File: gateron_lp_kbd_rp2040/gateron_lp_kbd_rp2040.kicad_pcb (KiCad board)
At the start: 2 copper layers, 234.5 x 116.5 mm, 244 parts, among them J1 TYPE-C-31-M-12, J2 Battery JST-SH, Q1 DMG3415U, SW1 KS-33, SW10 KS-33, SW11 KS-33, SW12 KS-33, SW13 KS-33, SW14 KS-33, SW15 KS-33, SW16 KS-33, SW17 KS-33, SW18 KS-33, SW19 KS-33, SW2 KS-33, SW20 KS-33, SW21 KS-33, SW22 KS-33, SW23 KS-33, SW24 KS-33, SW25 KS-33, SW26 KS-33, SW27 KS-33, SW28 KS-33, SW29 KS-33, SW3 KS-33, SW30 KS-33, SW31 KS-33, SW32 KS-33, SW33 KS-33, SW34 KS-33, SW35 KS-33, SW36 KS-33, SW37 KS-33, SW38 KS-33, SW39 KS-33, SW4 KS-33, SW40 KS-33, SW41 KS-33, SW42 KS-33, SW43 KS-33, SW44 KS-33, SW45 KS-33, SW46 KS-33, SW47 KS-33, SW48 KS-33, SW49 KS-33, SW5 KS-33, SW50 KS-33, SW51 KS-33, SW52 KS-33, SW53 KS-33, SW54 KS-33, SW55 KS-33, SW56 KS-33, SW57 KS-33, SW58 KS-33, SW59 KS-33, SW6 KS-33, SW60 RESET, SW61 BOOTSEL, SW62 PWR MSK-12C02, SW7 KS-33, SW8 KS-33, SW9 KS-33, U1 RP2040, U2 MCP73831, U3 AP2112K-3.3, U4 USBLC6-2SC6, U5 W25Q16JVUXIQ, U6 CYW43439, U7 74AHCT1G125, Y1 12MHz, Y2 37.4MHz

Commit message: Ground CYW43439 antenna matching in Raspberry Pi's real Pico W design
Cross-checked L2/C17/C18 and the crystal load caps against Raspberry Pi's
public Pico W hardware design files (same CYW43439 die, confirms 37.4MHz).
Real component families found there: 4.7nH match inductor, 27pF crystal
load caps, and a documented 0.2-2pF antenna tuning-cap family -- Pico W's
own BOM shows even Raspberry Pi tunes this network per-board rather than
using one fixed value, so C18 is left DNP pending real tuning here too.

Co-Authored-By: Claude Sonnet 5 <noreply@anthropic.com>
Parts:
- C17: value DNP (VERIFY) -> 1p (VERIFY, tune 0.2-2p)
- C18: value DNP (VERIFY) -> DNP (VERIFY, tune)
- C30, C31: value 18p -> 27p
- L2: value DNP (VERIFY) -> 4.7nH (ref: Pico W)
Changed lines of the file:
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@@
     (effects (font (size 1 1) (thickness 0.15)))
   )
-  (property "Value" "18p" (at 0 1.5 0) (layer "F.Fab")
+  (property "Value" "27p" (at 0 1.5 0) (layer "F.Fab")
     (effects (font (size 1 1) (thickness 0.15)))
   )
@@
     (effects (font (size 1 1) (thickness 0.15)))
   )
-  (property "Value" "18p" (at 0 1.5 0) (layer "F.Fab")
+  (property "Value" "27p" (at 0 1.5 0) (layer "F.Fab")
     (effects (font (size 1 1) (thickness 0.15)))
   )
@@
     (effects (font (size 1 1) (thickness 0.15)))
   )
-  (property "Value" "DNP (VERIFY)" (at 0 1.5 270) (layer "F.Fab")
+  (property "Value" "4.7nH (ref: Pico W)" (at 0 1.5 270) (layer "F.Fab")
     (effects (font (size 1 1) (thickness 0.15)))
   )
@@
     (effects (font (size 1 1) (thickness 0.15)))
   )
-  (property "Value" "DNP (VERIFY)" (at 0 1.5 0) (layer "F.Fab")
+  (property "Value" "1p (VERIFY, tune 0.2-2p)" (at 0 1.5 0) (layer "F.Fab")
     (effects (font (size 1 1) (thickness 0.15)))
   )
@@
     (effects (font (size 1 1) (thickness 0.15)))
   )
-  (property "Value" "DNP (VERIFY)" (at 0 1.5 0) (layer "F.Fab")
+  (property "Value" "DNP (VERIFY, tune)" (at 0 1.5 0) (layer "F.Fab")
     (effects (font (size 1 1) (thickness 0.15)))
   )

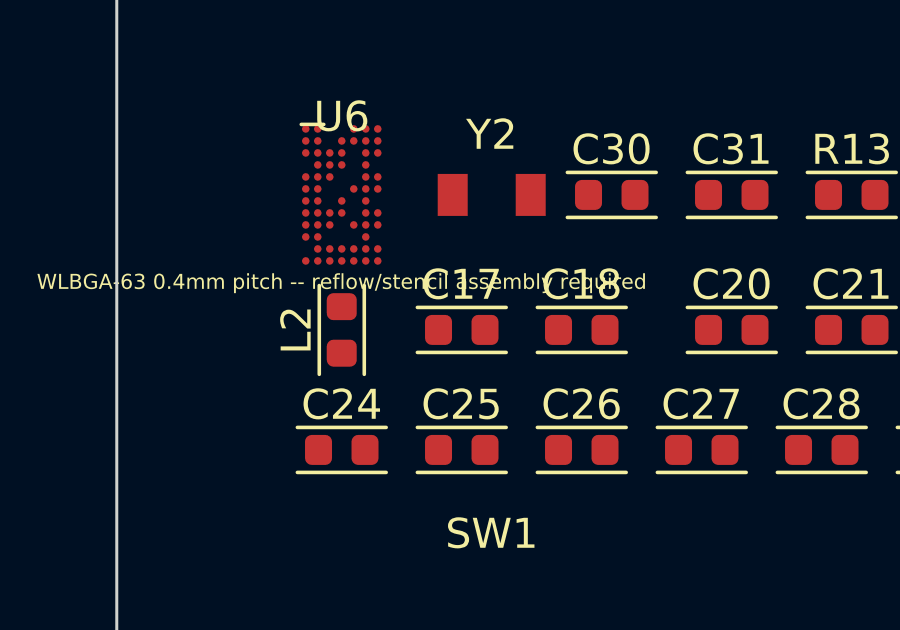
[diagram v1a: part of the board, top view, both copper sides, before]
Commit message: Match antenna-network footprints to real component package sizes
L2/C17/C18 were using the generic 0603-imperial footprint shared by this
file's other passives, but the real Pico W reference parts are smaller:
the antenna-match inductor is 0201 imperial (Murata LQP03TN4N7H02D, the
DigiKey-listed substitute for the now-obsolete Cyntec original) and the
Murata GJM1555C1H tuning-cap family is 0402 imperial. Added fp_0201/
fp_0402 land patterns and switched L2 to 0201, C17/C18 to 0402.

Co-Authored-By: Claude Sonnet 5 <noreply@anthropic.com>
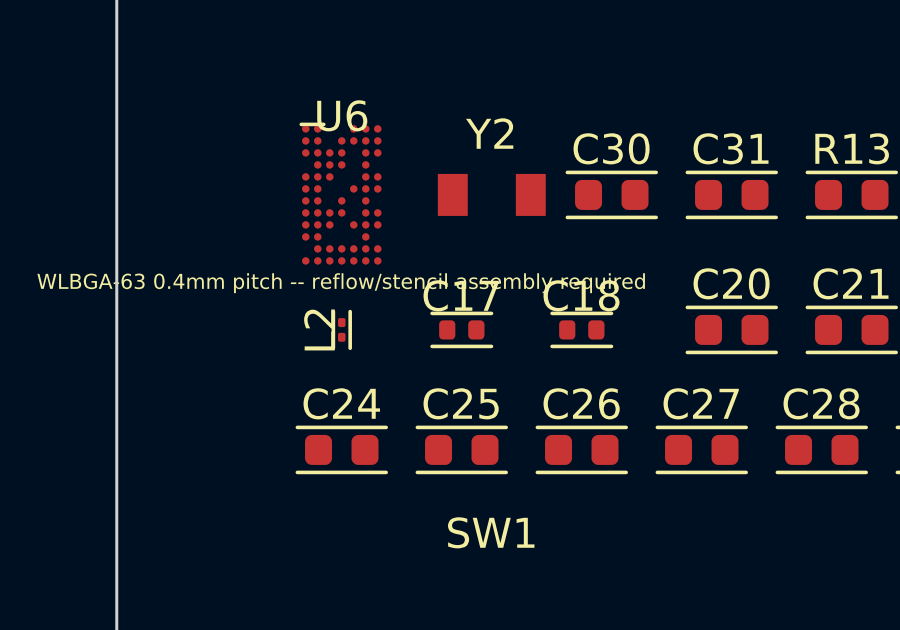
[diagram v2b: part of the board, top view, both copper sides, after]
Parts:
- C17, C18: footprint kbd:RC_0603 -> kbd:RC_0402
- L2: footprint kbd:RC_0603 -> kbd:RC_0201
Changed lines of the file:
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@@
     (fp_rect (start -1.5 -0.9) (end 1.5 0.9) (stroke (width 0.05) (type solid)) (fill none) (layer "F.CrtYd"))
   )
-  (footprint "kbd:RC_0603" (layer "F.Cu")
+  (footprint "kbd:RC_0201" (layer "F.Cu")
   (at 45 34.5 90)
-  (property "Reference" "L2" (at 0 -1.5 270) (layer "F.SilkS")
+  (property "Reference" "L2" (at 0 -0.7 270) (layer "F.SilkS")
     (effects (font (size 1 1) (thickness 0.15)))
   )
-  (property "Value" "4.7nH (ref: Pico W)" (at 0 1.5 270) (layer "F.Fab")
+  (property "Value" "4.7nH (ref: Pico W)" (at 0 0.7 270) (layer "F.Fab")
     (effects (font (size 1 1) (thickness 0.15)))
   )
-  (property "Footprint" "kbd:RC_0603" (at 0 0 0) (layer "F.Fab") (hide yes)
+  (property "Footprint" "kbd:RC_0201" (at 0 0 0) (layer "F.Fab") (hide yes)
     (effects (font (size 1.27 1.27))))
   (property "Datasheet" "" (at 0 0 0) (layer "F.Fab") (hide yes)
@@
     (effects (font (size 1.27 1.27))))
   (attr smd)
-    (pad "1" smd roundrect (at -0.775 0 90) (size 0.9 1) (layers "F.Cu" "F.Paste" "F.Mask") (net 46 "WLRF_ANT") (roundrect_rratio 0.25))
-    (pad "2" smd roundrect (at 0.775 0 90) (size 0.9 1) (layers "F.Cu" "F.Paste" "F.Mask") (net 47 "WLRF_ANT_MID") (roundrect_rratio 0.25))
-    (fp_rect (start -0.8 -0.4) (end 0.8 0.4) (stroke (width 0.1) (type solid)) (fill none) (layer "F.Fab"))
-    (fp_line (start -1.48 -0.75) (end 1.48 -0.75) (stroke (width 0.12) (type solid)) (layer "F.SilkS"))
-    (fp_line (start -1.48 0.75) (end 1.48 0.75) (stroke (width 0.12) (type solid)) (layer "F.SilkS"))
-    (fp_rect (start -1.5 -0.9) (end 1.5 0.9) (stroke (width 0.05) (type solid)) (fill none) (layer "F.CrtYd"))
+    (pad "1" smd roundrect (at -0.245 0 90) (size 0.3 0.25) (layers "F.Cu" "F.Paste" "F.Mask") (net 46 "WLRF_ANT") (roundrect_rratio 0.25))
+    (pad "2" smd roundrect (at 0.245 0 90) (size 0.3 0.25) (layers "F.Cu" "F.Paste" "F.Mask") (net 47 "WLRF_ANT_MID") (roundrect_rratio 0.25))
+    (fp_rect (start -0.3 -0.15) (end 0.3 0.15) (stroke (width 0.1) (type solid)) (fill none) (layer "F.Fab"))
+    (fp_line (start -0.61 -0.28) (end 0.61 -0.28) (stroke (width 0.12) (type solid)) (layer "F.SilkS"))
+    (fp_line (start -0.61 0.28) (end 0.61 0.28) (stroke (width 0.12) (type solid)) (layer "F.SilkS"))
+    (fp_rect (start -0.61 -0.33) (end 0.61 0.33) (stroke (width 0.05) (type solid)) (fill none) (layer "F.CrtYd"))
   )
-  (footprint "kbd:RC_0603" (layer "F.Cu")
+  (footprint "kbd:RC_0402" (layer "F.Cu")
   (at 49 34.5)
-  (property "Reference" "C17" (at 0 -1.5 0) (layer "F.SilkS")
+  (property "Reference" "C17" (at 0 -1.1 0) (layer "F.SilkS")
     (effects (font (size 1 1) (thickness 0.15)))
   )
-  (property "Value" "1p (VERIFY, tune 0.2-2p)" (at 0 1.5 0) (layer "F.Fab")
+  (property "Value" "1p (VERIFY, tune 0.2-2p)" (at 0 1.1 0) (layer "F.Fab")
     (effects (font (size 1 1) (thickness 0.15)))
   )
-  (property "Footprint" "kbd:RC_0603" (at 0 0 0) (layer "F.Fab") (hide yes)
+  (property "Footprint" "kbd:RC_0402" (at 0 0 0) (layer "F.Fab") (hide yes)
     (effects (font (size 1.27 1.27))))
   (property "Datasheet" "" (at 0 0 0) (layer "F.Fab") (hide yes)
@@
     (effects (font (size 1.27 1.27))))
   (attr smd)
-    (pad "1" smd roundrect (at -0.775 0) (size 0.9 1) (layers "F.Cu" "F.Paste" "F.Mask") (net 46 "WLRF_ANT") (roundrect_rratio 0.25))
-    (pad "2" smd roundrect (at 0.775 0) (size 0.9 1) (layers "F.Cu" "F.Paste" "F.Mask") (net 1 "GND") (roundrect_rratio 0.25))
-    (fp_rect (start -0.8 -0.4) (end 0.8 0.4) (stroke (width 0.1) (type solid)) (fill none) (layer "F.Fab"))
-    (fp_line (start -1.48 -0.75) (end 1.48 -0.75) (stroke (width 0.12) (type solid)) (layer "F.SilkS"))
-    (fp_line (start -1.48 0.75) (end 1.48 0.75) (stroke (width 0.12) (type solid)) (layer "F.SilkS"))
-    (fp_rect (start -1.5 -0.9) (end 1.5 0.9) (stroke (width 0.05) (type solid)) (fill none) (layer "F.CrtYd"))
+    (pad "1" smd roundrect (at -0.485 0) (size 0.54 0.64) (layers "F.Cu" "F.Paste" "F.Mask") (net 46 "WLRF_ANT") (roundrect_rratio 0.25))
+    (pad "2" smd roundrect (at 0.485 0) (size 0.54 0.64) (layers "F.Cu" "F.Paste" "F.Mask") (net 1 "GND") (roundrect_rratio 0.25))
+    (fp_rect (start -0.5 -0.25) (end 0.5 0.25) (stroke (width 0.1) (type solid)) (fill none) (layer "F.Fab"))
+    (fp_line (start -0.99 -0.55) (end 0.99 -0.55) (stroke (width 0.12) (type solid)) (layer "F.SilkS"))
+    (fp_line (start -0.99 0.55) (end 0.99 0.55) (stroke (width 0.12) (type solid)) (layer "F.SilkS"))
+    (fp_rect (start -1 -0.6) (end 1 0.6) (stroke (width 0.05) (type solid)) (fill none) (layer "F.CrtYd"))
   )
-  (footprint "kbd:RC_0603" (layer "F.Cu")
+  (footprint "kbd:RC_0402" (layer "F.Cu")
   (at 53 34.5)
-  (property "Reference" "C18" (at 0 -1.5 0) (layer "F.SilkS")
+  (property "Reference" "C18" (at 0 -1.1 0) (layer "F.SilkS")
     (effects (font (size 1 1) (thickness 0.15)))
   )
-  (property "Value" "DNP (VERIFY, tune)" (at 0 1.5 0) (layer "F.Fab")
+  (property "Value" "DNP (VERIFY, tune)" (at 0 1.1 0) (layer "F.Fab")
     (effects (font (size 1 1) (thickness 0.15)))
   )
-  (property "Footprint" "kbd:RC_0603" (at 0 0 0) (layer "F.Fab") (hide yes)
+  (property "Footprint" "kbd:RC_0402" (at 0 0 0) (layer "F.Fab") (hide yes)
     (effects (font (size 1.27 1.27))))
   (property "Datasheet" "" (at 0 0 0) (layer "F.Fab") (hide yes)
@@
     (effects (font (size 1.27 1.27))))
   (attr smd)
-    (pad "1" smd roundrect (at -0.775 0) (size 0.9 1) (layers "F.Cu" "F.Paste" "F.Mask") (net 47 "WLRF_ANT_MID") (roundrect_rratio 0.25))
-    (pad "2" smd roundrect (at 0.775 0) (size 0.9 1) (layers "F.Cu" "F.Paste" "F.Mask") (net 1 "GND") (roundrect_rratio 0.25))
-    (fp_rect (start -0.8 -0.4) (end 0.8 0.4) (stroke (width 0.1) (type solid)) (fill none) (layer "F.Fab"))
-    (fp_line (start -1.48 -0.75) (end 1.48 -0.75) (stroke (width 0.12) (type solid)) (layer "F.SilkS"))
-    (fp_line (start -1.48 0.75) (end 1.48 0.75) (stroke (width 0.12) (type solid)) (layer "F.SilkS"))
-    (fp_rect (start -1.5 -0.9) (end 1.5 0.9) (stroke (width 0.05) (type solid)) (fill none) (layer "F.CrtYd"))
+    (pad "1" smd roundrect (at -0.485 0) (size 0.54 0.64) (layers "F.Cu" "F.Paste" "F.Mask") (net 47 "WLRF_ANT_MID") (roundrect_rratio 0.25))
+    (pad "2" smd roundrect (at 0.485 0) (size 0.54 0.64) (layers "F.Cu" "F.Paste" "F.Mask") (net 1 "GND") (roundrect_rratio 0.25))
+    (fp_rect (start -0.5 -0.25) (end 0.5 0.25) (stroke (width 0.1) (type solid)) (fill none) (layer "F.Fab"))
+    (fp_line (start -0.99 -0.55) (end 0.99 -0.55) (stroke (width 0.12) (type solid)) (layer "F.SilkS"))
+    (fp_line (start -0.99 0.55) (end 0.99 0.55) (stroke (width 0.12) (type solid)) (layer "F.SilkS"))
+    (fp_rect (start -1 -0.6) (end 1 0.6) (stroke (width 0.05) (type solid)) (fill none) (layer "F.CrtYd"))
   )
   (footprint "kbd:RC_0603" (layer "F.Cu")

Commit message: Confirm crystal load caps and series resistor against Pico W reference
C30/C31 (27pF) and R13 (0R) were already set to these values but flagged
VERIFY -- re-checked against Raspberry Pi's public Pico W design files
with reference-designator-level evidence this time (not just proximity in
the raw dump): C257/C258 map 1:1 to the 27pF footprint, exactly the pair
a crystal load network needs, and a 0R chip resistor sits on the wireless
chip's crystal clock net. 27pF externals also check out physically
(~15.5-18.5pF effective load cap with typical stray, a standard CL rating).
No value changes, just upgraded confidence and updated comments.

Co-Authored-By: Claude Sonnet 5 <noreply@anthropic.com>
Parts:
- R13: value 0 (VERIFY) -> 0 (ref: Pico W)
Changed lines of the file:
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@@
     (effects (font (size 1 1) (thickness 0.15)))
   )
-  (property "Value" "0 (VERIFY)" (at 0 1.5 0) (layer "F.Fab")
+  (property "Value" "0 (ref: Pico W)" (at 0 1.5 0) (layer "F.Fab")
     (effects (font (size 1 1) (thickness 0.15)))
   )

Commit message: Verify RP2040 pin numbers against the real datasheet, fix two real bugs
Pin numbers, dedicated-pin names, and QFN-56 side rotation now come from
Raspberry Pi's own RP2040 datasheet (Fig. 3, Table 1, Table 2) instead of
an invented sequential scheme. This caught two real design bugs:

- The core supply was modeled as a buck regulator needing an external
  inductor (L1, 2.2uH). The real on-chip regulator (Section 2.10, "Core
  Supply Regulator") is a linear/LDO type -- VREG_VIN -> VREG_VOUT -> DVDD
  -- needing only decoupling capacitors. L1 is removed; C9/C32/C33/C34 now
  match the datasheet's own application circuit (Figure 20).
- The BT UART was wired to GPIO18-21, but UART1's real alternate-function
  pins are GPIO20-23 (Table 2) -- GPIO18/19 (no alt-function needed) now
  carry BT_REG_ON/BT_DEV_WAKE instead, freeing GPIO20-23 for the actual
  UART1 TX/RX/CTS/RTS.

Also fixed: the real chip has no perimeter GND pins (GND is only the
single exposed thermal pad) -- removed several invented ones. And caught,
independently of the pinout work, two schematic label collisions (C13/C14
and C30/C31 crystal load caps landing global labels of different nets on
the identical coordinate, which can short a net to GND in the extracted
netlist) -- widened spacing to fix both.

Verified via kicad-happy analyzers: zero new errors/warnings, zero
courtyard or keepout collisions, zero schematic label collisions anywhere
in the file (full-file scan, not just the touched areas).

Co-Authored-By: Claude Sonnet 5 <noreply@anthropic.com>
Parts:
- removed L1: 2.2uH, kbd:RC_0603
- added C32: 100n, kbd:RC_0603, F.Cu at (164.0, 24.5)
- added C33: 100n, kbd:RC_0603, F.Cu at (168.0, 24.5)
- added C34: 1u, kbd:RC_0603, F.Cu at (172.0, 24.5)
- C9: value 10u -> 1u
- moved C10 8.00 mm to (176.0, 24.5)
- moved C11 8.00 mm to (180.0, 24.5)
- moved C12 8.00 mm to (188.0, 24.5)
- moved R9 8.00 mm to (184.0, 24.5)
- moved C9 4.00 mm to (160.0, 24.5)
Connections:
- C9 pad 1: VDD_CORE -> DVDD
- U1 pad 1: ROW0 -> +3V3
- U1 pad 10: COL4 -> +3V3
- U1 pad 11: COL5 -> COL3
- U1 pad 12: COL6 -> COL4
- U1 pad 13: COL7 -> COL5
- U1 pad 14: COL8 -> COL6
- U1 pad 15: COL9 -> COL7
- U1 pad 16: COL10 -> COL8
- U1 pad 17: COL11 -> COL9
- U1 pad 18: RGB_GPIO -> COL10
- U1 pad 2: ROW1 -> ROW0
- U1 pad 20: GND -> XIN
- U1 pad 21: USB_DM -> XOUT
- U1 pad 22: USB_DP -> +3V3
- U1 pad 23: QSPI_SCLK -> DVDD
- U1 pad 24: QSPI_SD0 -> SWCLK
- U1 pad 25: QSPI_SD1 -> SWDIO
- U1 pad 26: QSPI_SD2 -> RUN
- U1 pad 27: QSPI_SD3 -> COL11
- U1 pad 28: QSPI_SS -> RGB_GPIO
- U1 pad 29: XIN -> BT_REG_ON
- U1 pad 3: ROW2 -> ROW1
- U1 pad 30: XOUT -> BT_DEV_WAKE
- U1 pad 31: GND -> BT_UART_RXD
- U1 pad 32: +3V3 -> BT_UART_TXD
- U1 pad 33: GND -> +3V3
- U1 pad 34: RUN -> BT_UART_RTS_N
- U1 pad 35: SWCLK -> BT_UART_CTS_N
- U1 pad 36: SWDIO -> (no net)
- U1 pad 37: VDD_CORE -> (no net)
- U1 pad 38: GND -> VBAT_SENSE
- U1 pad 39: BT_UART_RXD -> (no net)
- U1 pad 4: ROW3 -> ROW2
- U1 pad 40: BT_UART_TXD -> BT_HOST_WAKE
- U1 pad 41: BT_UART_CTS_N -> (no net)
- U1 pad 42: BT_UART_RTS_N -> +3V3
- U1 pad 43: BT_REG_ON -> +3V3
- U1 pad 44: BT_DEV_WAKE -> VREG_VIN
- U1 pad 45: VBAT_SENSE -> DVDD
- U1 pad 46: (no net) -> USB_DM
- U1 pad 47: BT_HOST_WAKE -> USB_DP
- U1 pad 48: (no net) -> +3V3
- U1 pad 5: ROW4 -> ROW3
- U1 pad 50: +3V3 -> DVDD
- U1 pad 51: GND -> QSPI_SD3
- U1 pad 52: GND -> QSPI_SCLK
- U1 pad 53: GND -> QSPI_SD0
- U1 pad 54: GND -> QSPI_SD2
- U1 pad 55: +3V3 -> QSPI_SD1
- U1 pad 56: +3V3 -> QSPI_SS
- U1 pad 6: COL0 -> ROW4
- U1 pad 7: COL1 -> COL0
- U1 pad 8: COL2 -> COL1
- U1 pad 9: COL3 -> COL2
